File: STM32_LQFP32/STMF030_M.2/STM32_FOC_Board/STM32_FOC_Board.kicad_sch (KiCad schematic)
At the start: 37 parts, among them J1 Bus_M.2_Socket_E, SW1 TS342A2P-WZ, SW2 TS342A2P-WZ, U1 STM32F446RETx, U2 ME6217C33M5G, X1 FC-12M32.768KHZ7PF20PPM, X2 7R24000E12UBE

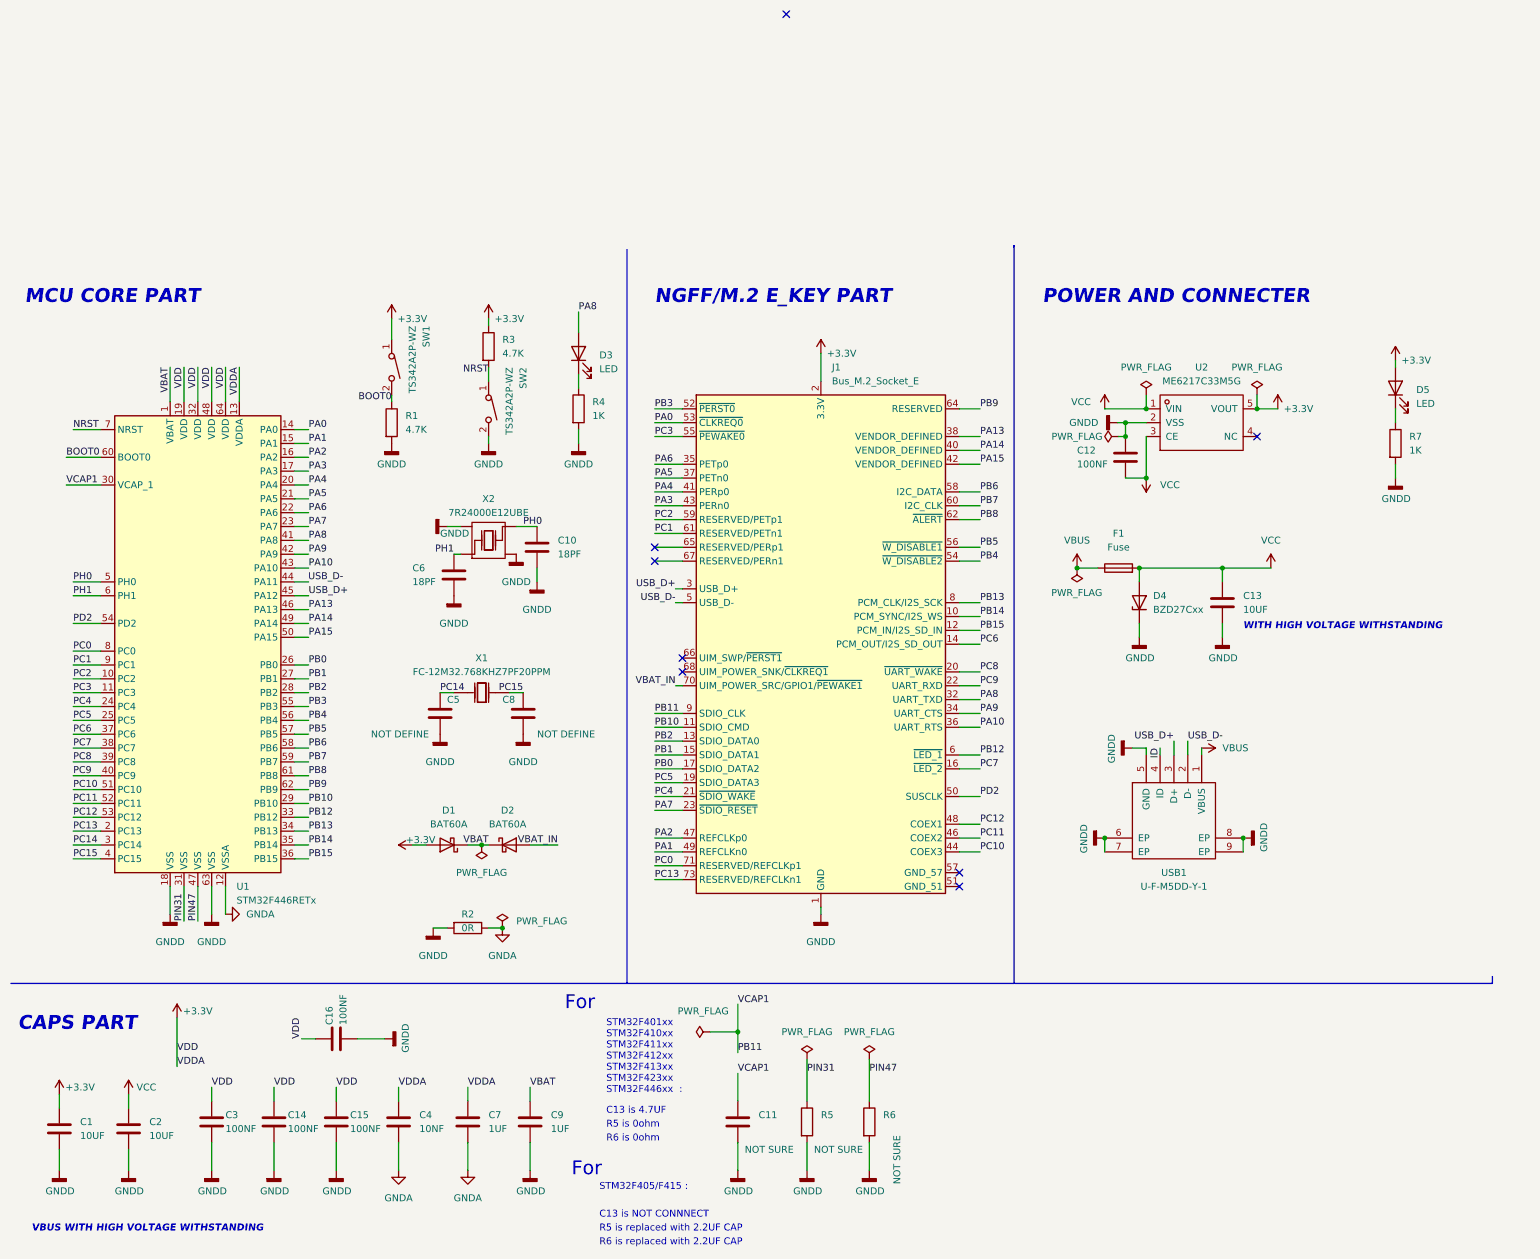
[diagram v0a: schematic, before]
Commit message: "UPDATE LQFP32 AND LQFP64"
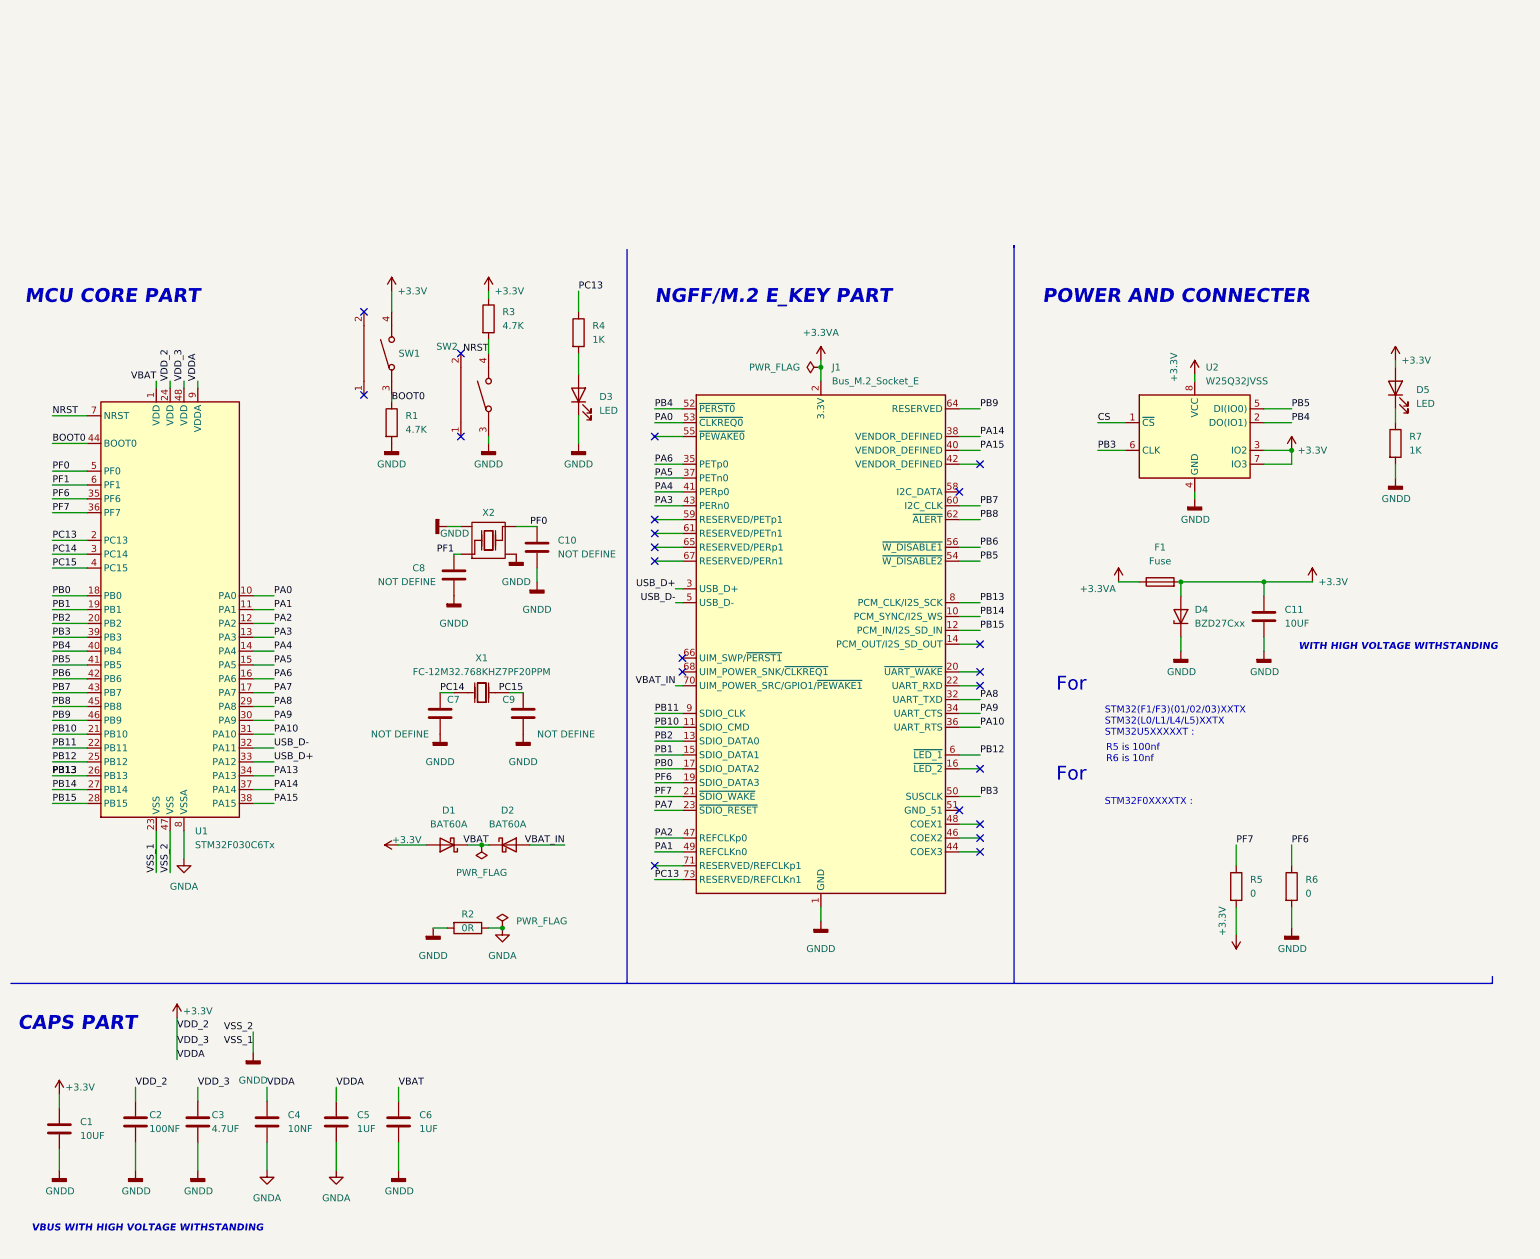
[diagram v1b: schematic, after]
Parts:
- removed C12, C14, C15, C16: 100NF, Capacitor_SMD:C_0402_1005Metric, symbol Device:C
- removed C13: 10UF, Capacitor_SMD:C_0603_1608Metric, symbol Device:C
- removed SW1, SW2: TS342A2P-WZ, kicad_lceda:SW-SMD_L4.0-W2.9-LS5.0, symbol kicad_lceda:TS342A2P-WZ
- removed U1: STM32F446RETx, Package_QFP:LQFP-64_10x10mm_P0.5mm, symbol MCU_ST_STM32F4:STM32F446RETx
- removed U2: ME6217C33M5G, kicad_lceda:SOT-23-5_L3.0-W1.7-P0.95-LS2.8-BR, symbol kicad_lceda:ME6217C33M5G
- removed USB1: U-F-M5DD-Y-1, kicad_lceda:MICRO-USB-SMD_U-F-M5DD-Y-1, symbol kicad_lceda:U-F-M5DD-Y-1
- added SW1, SW2: TS24CA, kicad_lceda:SW-SMD_TS24CA, symbol kicad_lceda:TS24CA
- added U1: STM32F030C6Tx, Package_QFP:LQFP-48_7x7mm_P0.5mm, symbol MCU_ST_STM32F0:STM32F030C6Tx
- added U2: W25Q32JVSS, Package_SO:SOIC-8_5.23x5.23mm_P1.27mm, symbol Memory_Flash:W25Q32JVSS
- C10: value 18PF -> NOT DEFINE
- C11: value NOT SURE -> 10UF; footprint Capacitor_SMD:C_0402_1005Metric -> Capacitor_SMD:C_0603_1608Metric
- C2: value 10UF -> 100NF; footprint Capacitor_SMD:C_0603_1608Metric -> Capacitor_SMD:C_0402_1005Metric
- C3: value 100NF -> 4.7UF
- C8: renamed from C6; value 18PF -> NOT DEFINE
- R1, R3, R4: footprint Resistor_SMD:R_0603_1608Metric -> Resistor_SMD:R_0402_1005Metric
- R5, R6: value NOT SURE -> 0
- X2: footprint kicad_lceda:CRYSTAL-SMD_4P-L1.6-W1.2-BL -> kicad_lceda:OSC-SMD_4P-L2.5-W2.0-BL.kicad_mod
- renumbered C7 to C5, C9 to C6, C5 to C7, C8 to C9
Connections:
- net PD2 is gone; now on net PB3: J1.50 (SUSCLK)
- net PIN31 is gone; now on net PF7: R5.1
- net PIN47 is gone; now on net PF6: R6.1
- net VCC is gone; now on net +3V3: C2.1, D4.2 (A), F1.2
- net +3V3: now also C11.1, R5.2, SW1.4, U1.24 (VDD), U1.48 (VDD), U1.9 (VDDA), U2.3 (IO2), U2.7 (IO3), U2.8 (VCC); no longer J1.2 (3.3V), J1.4 (3.3V), J1.72 (3.3V), J1.74 (3.3V)
- net BOOT0: now also SW1.3, U1.44 (BOOT0)
- net GNDA: now also U1.8 (VSSA)
- net GNDD: now also D3.1 (K), J1.57 (GND), SW2.3, U1.23 (VSS), U1.47 (VSS), U2.4 (GND); no longer R4.2, R5.2
- net NRST: now also SW2.4, U1.7 (NRST)
- net PA0: now also U1.10 (PA0)
- net PA1: now also U1.11 (PA1)
- net PA10: now also U1.31 (PA10)
- net PA13: now also U1.34 (PA13); no longer J1.38 (VENDOR_DEFINED)
- net PA14: now also J1.38 (VENDOR_DEFINED), U1.37 (PA14); no longer J1.40 (VENDOR_DEFINED)
- net PA15: now also J1.40 (VENDOR_DEFINED), U1.38 (PA15); no longer J1.42 (VENDOR_DEFINED)
- net PA2: now also U1.12 (PA2)
- net PA3: now also U1.13 (PA3)
- net PA4: now also U1.14 (PA4)
- net PA5: now also U1.15 (PA5)
- net PA6: now also U1.16 (PA6)
- net PA7: now also U1.17 (PA7)
- net PA8: now also U1.29 (PA8); no longer D3.2 (A)
- net PA9: now also U1.30 (PA9)
- net PB0: now also U1.18 (PB0)
- net PB1: now also U1.19 (PB1)
- net PB10: now also U1.21 (PB10)
- net PB11: now also U1.22 (PB11); no longer C11.1
- net PB12: now also U1.25 (PB12)
- net PB13: now also U1.26 (PB13)
- net PB14: now also U1.27 (PB14)
- net PB15: now also U1.28 (PB15)
- net PB2: now also U1.20 (PB2)
- net PB3: now also U1.39 (PB3), U2.6 (CLK); no longer J1.52 (~{PERST0})
- net PB4: now also J1.52 (~{PERST0}), U1.40 (PB4), U2.2 (DO(IO1)); no longer J1.54 (~{W_DISABLE2})
- net PB5: now also J1.54 (~{W_DISABLE2}), U1.41 (PB5), U2.5 (DI(IO0)); no longer J1.56 (~{W_DISABLE1})
- net PB6: now also J1.56 (~{W_DISABLE1}), U1.42 (PB6); no longer J1.58 (I2C_DATA)
- net PB7: now also U1.43 (PB7)
- net PB8: now also U1.45 (PB8)
- net PB9: now also U1.46 (PB9)
- net PC13: now also R4.1, U1.2 (PC13)
- net PC14: now also U1.3 (PC14)
- net PC15: now also U1.4 (PC15)
- net USB_D+: now also U1.33 (PA12)
- net USB_D-: now also U1.32 (PA11)
- net VBAT: now also U1.1 (VDD)
- net PC0: no longer names the net of J1.71 (RESERVED/REFCLKp1)
- net PC1: no longer names the net of J1.61 (RESERVED/PETn1)
- net PC10: no longer names the net of J1.44 (COEX3)
- net PC11: no longer names the net of J1.46 (COEX2)
- net PC12: no longer names the net of J1.48 (COEX1)
- net PC2: no longer names the net of J1.59 (RESERVED/PETp1)
- net PC3: no longer names the net of J1.55 (~{PEWAKE0})
- net PC4 renamed PF7
- net PF7: now also U1.36 (PF7)
- net PC5 renamed PF6
- net PF6: now also U1.35 (PF6)
- net PC6: no longer names the net of J1.14 (PCM_OUT/I2S_SD_OUT)
- net PC7: no longer names the net of J1.16 (~{LED_2})
- net PC8: no longer names the net of J1.20 (~{UART_WAKE})
- net PC9: no longer names the net of J1.22 (UART_RXD)
- net PH0 renamed PF0
- net PF0: now also U1.5 (PF0)
- net PH1 renamed PF1
- net PF1: now also U1.6 (PF1)
- net VBUS renamed +3.3VA
- net +3.3VA: now also J1.2 (3.3V), J1.4 (3.3V), J1.72 (3.3V), J1.74 (3.3V)
- new net: D3.2 (A), R4.2
- new net CS: U2.1 (~{CS})
- no-connect marks 8 -> 22
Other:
- note added: "R5 is 100nf R6 is 10nf"
- note added: "STM32(F1/F3)(01/02/03)XXTX STM32(L0/L1/L4/L5)XXTX STM32U5XXXXXT :"
- note added: "STM32F0XXXXTX :"
- note removed: "C13 is 4.7UF"
- note removed: "C13 is NOT CONNNECT"
- note removed: "R5 is 0ohm"
- note removed: "R5 is replaced with 2.2UF CAP"
- note removed: "R6 is 0ohm"
- note removed: "R6 is replaced with 2.2UF CAP"
- note removed: "STM32F401xx STM32F410xx STM32F411xx STM32F412xx STM32F413xx STM32F423xx STM32F446xx :"
- note removed: "STM32F405/F415 :"
- title: STM32_M.2_E_KEY_LQFP-64_USB -> STM32_M.2_E_KEY_LQFP-48_HC
- moved on the sheet: C4, C5, C6, D3, R3, R4
